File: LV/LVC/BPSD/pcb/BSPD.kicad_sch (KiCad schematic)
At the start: 12 parts, among them J1 Conn_01x05_Pin, U1 LM339, U2 74LS08

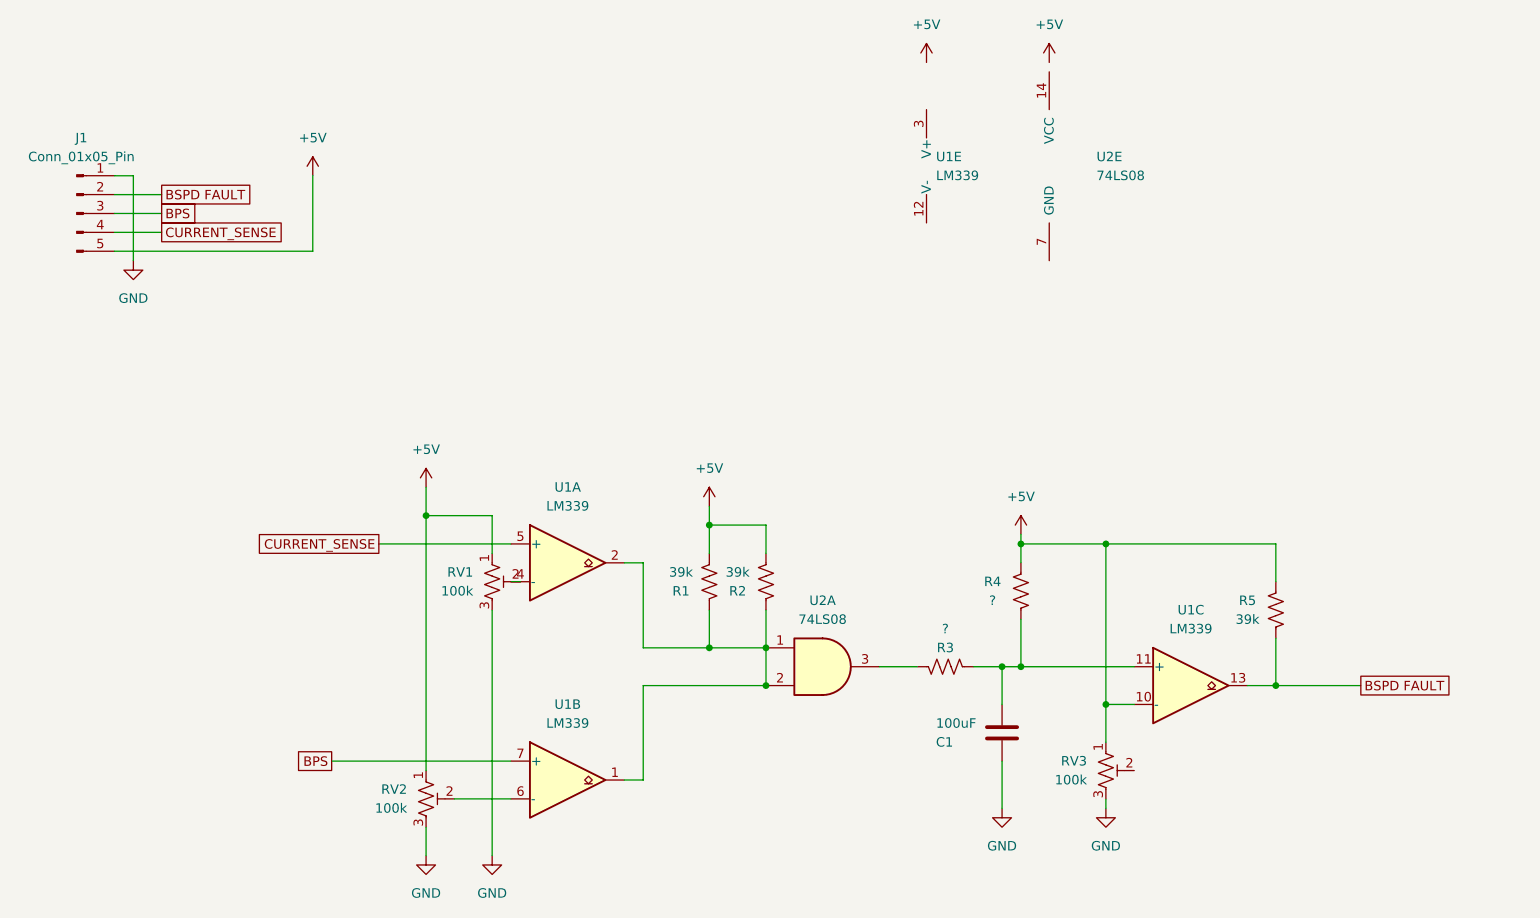
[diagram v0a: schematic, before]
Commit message: updated bpsd circuit
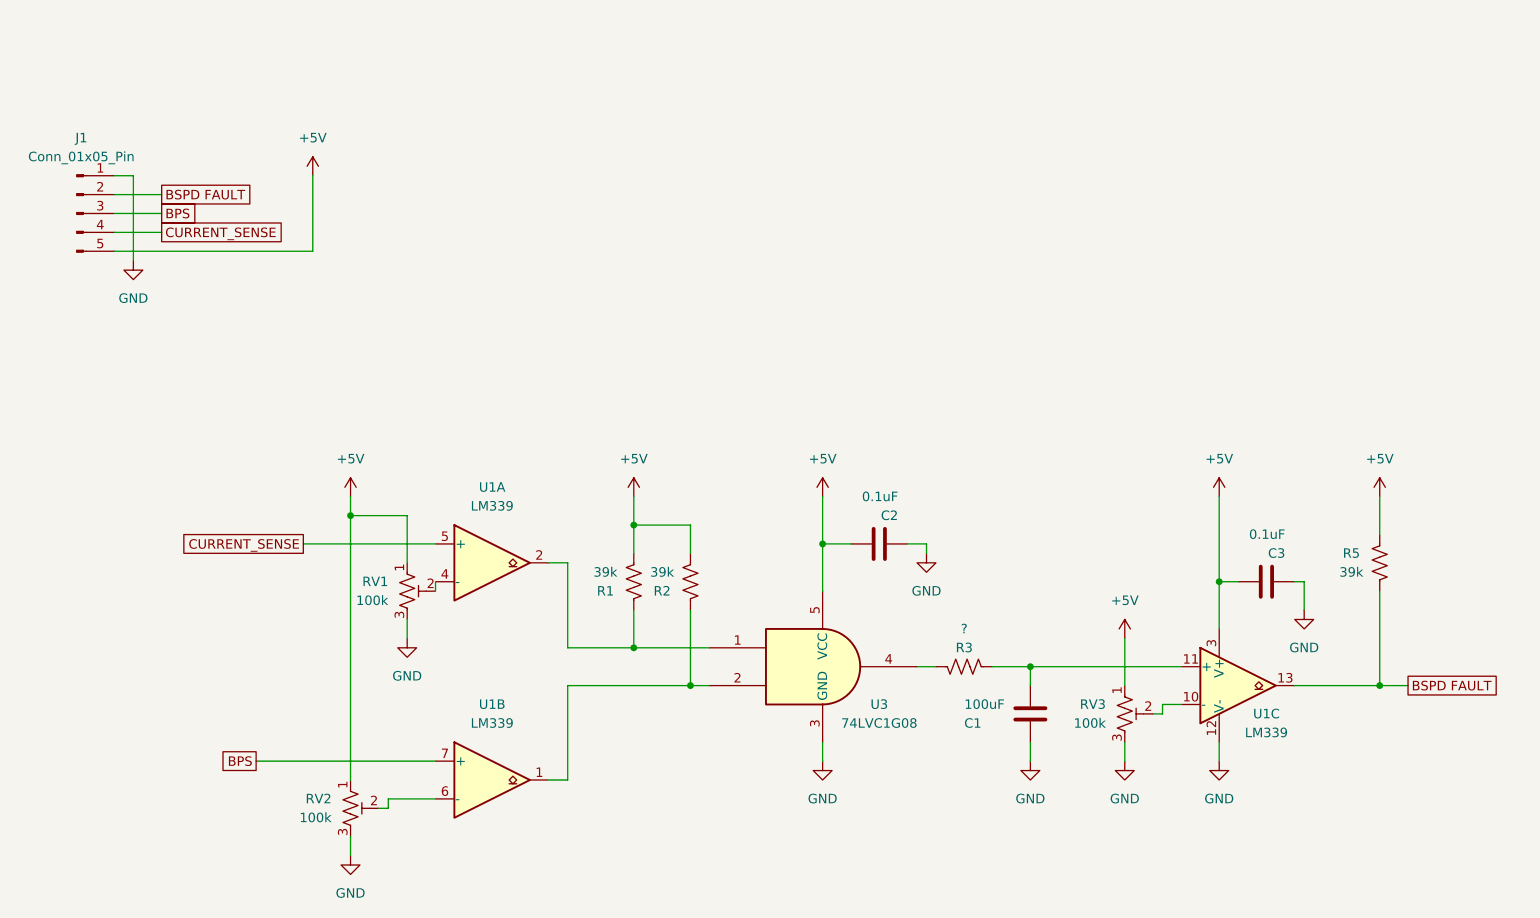
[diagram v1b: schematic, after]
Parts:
- removed R4: ?, Resistor_THT:R_Axial_DIN0204_L3.6mm_D1.6mm_P5.08mm_Horizontal, symbol Device:R_US
- removed U2: 74LS08, symbol 74xx:74LS08
- added C2, C3: 0.1uF, Capacitor_THT:C_Rect_L7.5mm_W6.5mm_P5.00mm, symbol Device:C
- added U3: 74LVC1G08, Package_TO_SOT_SMD:SOT-23-5_HandSoldering, symbol 74xGxx:74LVC1G08
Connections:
- net +5V: now also U1.3 (V+), C2.1, C3.1, U3.5 (VCC); no longer U1.10 (-)
- net GND: now also U1.12 (V-), C2.2, C3.2, U3.3 (GND)
- net at R2.2, U1.1: now also U3.2; no longer R1.2, U1.2
- net at RV3.2: now also U1.10 (-)
- net at R3.2: now also U3.4
- new net: R1.2, U1.2, U3.1
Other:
- moved on the sheet: C1, R1, R2, R3, R5, RV1, RV2, RV3, U1A, U1B, U1C
